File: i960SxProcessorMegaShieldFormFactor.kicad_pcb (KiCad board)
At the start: 4 copper layers, 101.6 x 53.3 mm, 42 parts, among them P1 Power, P2 Data Lines Lower, P3 Data Lines Upper, P4 Address Lines, P5 PWM, P6 Serializable Pins, P7 1284p Direct Connection, U1 74LVC16T245, U2 74AHC16373, U3 80960Sx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

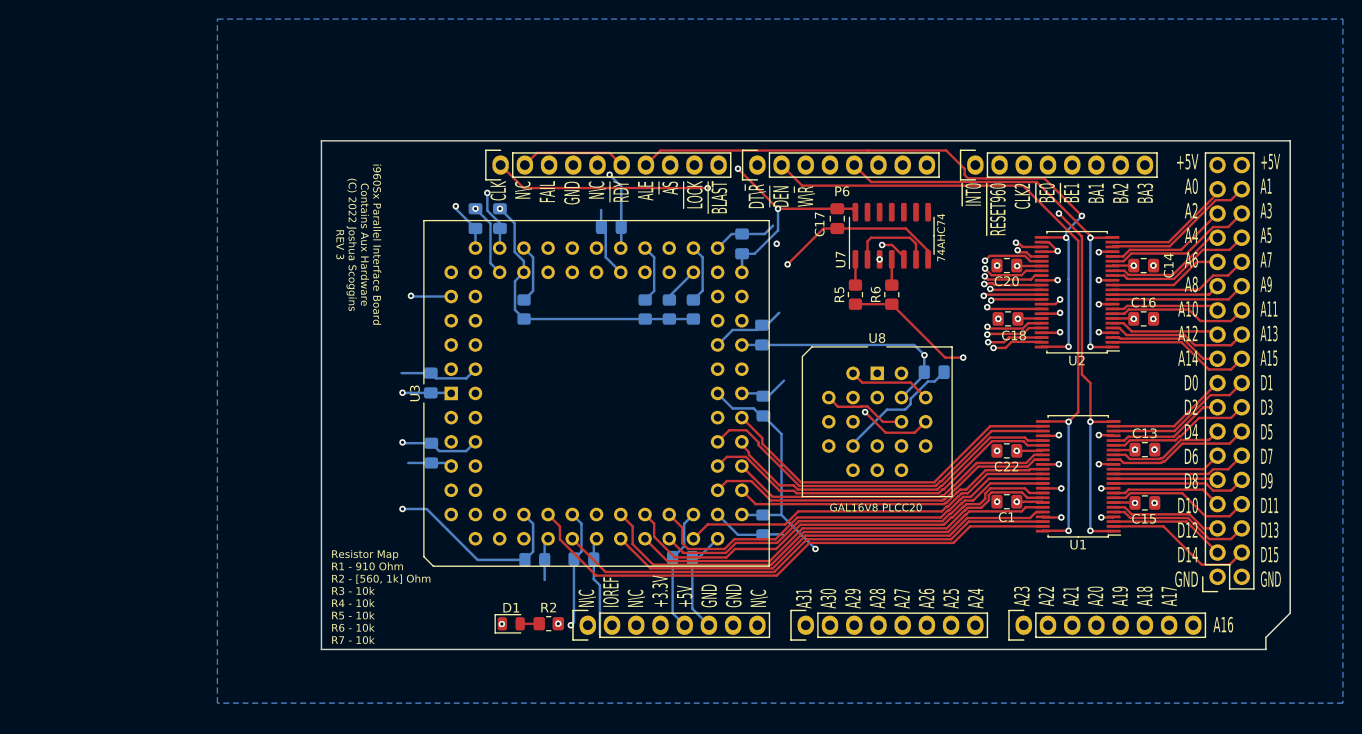
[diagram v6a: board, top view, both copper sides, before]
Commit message: Clean up all of the aux hardware and put the capacitors in the area underneath the socket
It makes it much cleaner

Also, I made sure that the ground and power planes are on all layers to
reduce complexity
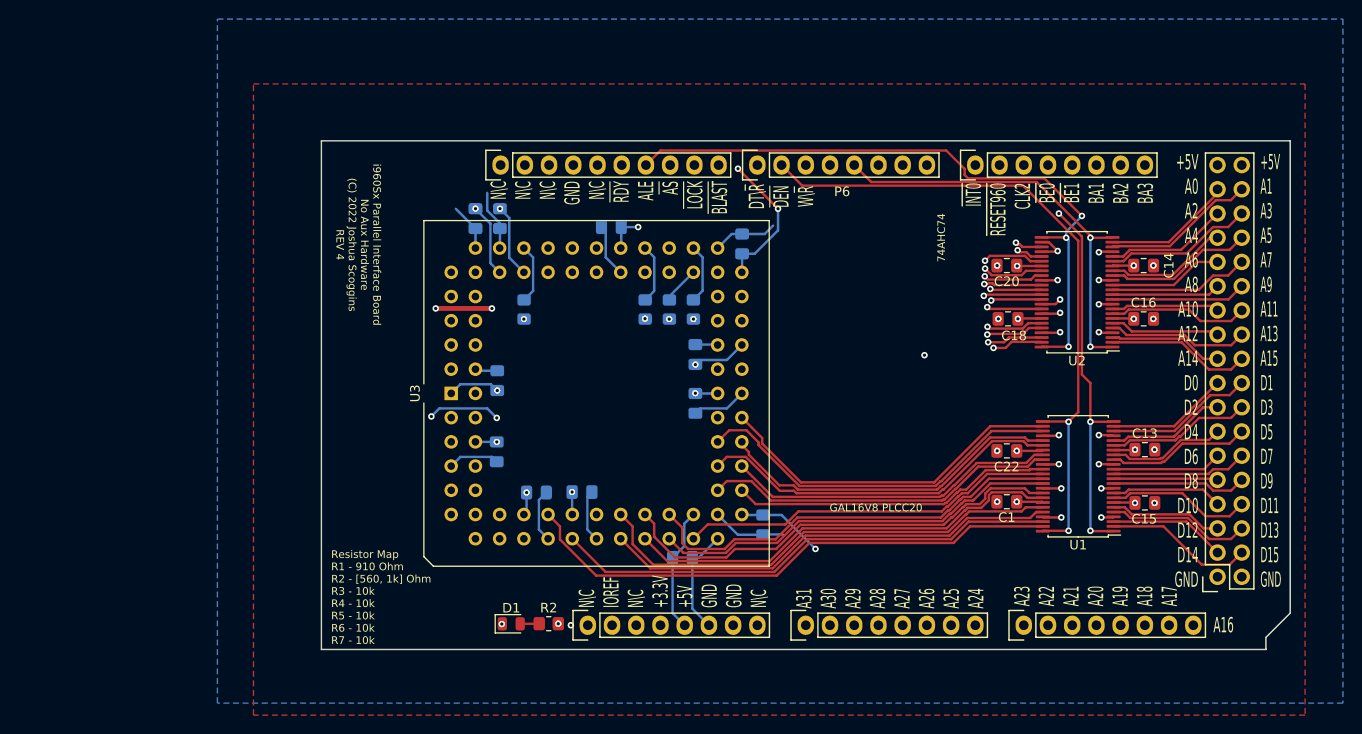
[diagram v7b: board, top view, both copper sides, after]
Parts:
- removed C17, C19: 0.1uF, Capacitor_SMD:C_0805_2012Metric_Pad1.18x1.45mm_HandSolder
- removed R5, R6: 10k, Resistor_SMD:R_0805_2012Metric_Pad1.20x1.40mm_HandSolder
- removed U7: 74AHC74, Package_SO:SOIC-14_3.9x8.7mm_P1.27mm
- removed U8: GAL16V8, Package_LCC:PLCC-20_THT-Socket
- moved C12 7.28 mm to (142.6, 90.7)
- moved C21 7.14 mm to (142.6, 95.9), turned to -90 degrees
- moved C4 7.07 mm to (125.9, 105.2)
- moved C3 7.04 mm to (130.7, 105.2)
- moved C7 6.98 mm to (121.8, 93.5)
- moved C5 6.87 mm to (121.8, 100.9)
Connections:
- P5 pad 1: /CLK_DIV2 -> unconnected-(P5-Pad1)
- P5 pad 2: /~{READY} -> unconnected-(P5-Pad2)
- P5 pad 3: /MCU_FAIL -> unconnected-(P5-Pad3)
- U3 pad 79: /~{READY960} -> /~{READY}
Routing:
- net +5V: track 200.2 -> 88.7 mm, vias 14 -> 22
- net /CLK_DIV2: track 61.3 -> 0.00 mm, vias 3 -> 0
- net /MCU_FAIL: track 60.1 -> 0.00 mm, vias 1 -> 0
- net /~{READY960}: track 58.7 -> 0.00 mm
- net GND: track 149.7 -> 105.7 mm, vias 29 -> 27
- net /~{BLAST}\~{FAIL}: track 65.3 -> 25.6 mm
- net /~{READY}: track 51.3 -> 28.4 mm
- net /~{BE0}: track 60.0 -> 40.4 mm
- net /~{BE1}: track 57.3 -> 40.4 mm
- net Net-(U7-Pad2): track 9.03 -> 0.00 mm
- net /Sheet62305775/X: track 8.70 -> 0.00 mm
- net /Sheet62305775/Z: track 8.67 -> 0.00 mm
- net /Sheet62305775/~{SR0}: track 2.70 -> 0.00 mm
- net /Sheet62305775/~{MR0}: track 2.70 -> 0.00 mm
- net /CLKO: vias 1 -> 0
- added copper zone on F.Cu, net +5V
- added copper zone on In1.Cu, net +5V
- added copper zone on In2.Cu, net GND
- removed copper zone on In2.Cu, net +5V
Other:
- board text added: "N\C N\C N\C GND N\C ~{RDY} ALE ~{AS} ~{LOCK} ~{BLAST}"
- board text added: "i960Sx Parallel Interface Board No Aux Hardware (C) 2022 Joshua Scoggins REV 4"
- board text removed: "CLK N\C FAIL GND N\C ~{RDY} ALE ~{AS} ~{LOCK} ~{BLAST}"
- board text removed: "GAL16V8 Synchronizer CLK S Z X B0 B1 BL NC NC GND NC NC NC NC NC FL X0 Z0 RDY VCC Z0.R = S X0.R = Z /RDY = X * /Z FL.R = B0 * B1 * /BL DESCRIPTION i960 Aux Hardware"
- board text removed: "i960Sx Parallel Interface Board Contains Aux Hardware (C) 2022 Joshua Scoggins REV 3"

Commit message: Finished wiring
Super easy this way :)
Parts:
- moved C10 14.5 mm to (148.3, 77.1)
- moved C11 14.5 mm to (162.0, 78.9)
- moved C12 14.5 mm to (157.1, 90.5)
- moved C2 14.5 mm to (155.7, 111.8)
- moved C21 14.5 mm to (157.1, 95.6)
- moved C4 14.5 mm to (140.4, 105.0)
- moved C6 14.5 mm to (164.2, 108.4)
- moved C7 14.5 mm to (136.3, 93.2)
- moved R3 14.5 mm to (151.8, 85.8)
- moved R4 14.5 mm to (154.4, 85.8)
- moved R7 14.5 mm to (156.9, 85.8)
- moved U3 14.5 mm to (131.5, 94.6)
- moved C5 14.5 mm to (136.2, 100.7)
- moved C8 14.5 mm to (134.0, 76.3)
- moved C9 14.5 mm to (136.6, 76.3)
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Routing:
- net VCC: track 136.8 -> 36.9 mm
- net GND: track 105.7 -> 141.8 mm, vias 27 -> 21
- net /AD11: track 111.7 -> 79.0 mm
- net /AD1: track 87.4 -> 58.0 mm
- net /AD10: track 111.4 -> 82.5 mm
- net /AD3: track 87.4 -> 58.5 mm
- net /AD2: track 81.5 -> 52.7 mm
- net /AD12: track 116.4 -> 87.7 mm
- net /AD8: track 105.5 -> 77.2 mm
- net /AD4: track 81.1 -> 53.0 mm
- net /AD9: track 101.8 -> 73.9 mm
- net /AD14: track 122.0 -> 94.2 mm
- net /AD13: track 112.1 -> 84.4 mm
- net /AD5: track 87.1 -> 59.9 mm
- net /AD15: track 131.1 -> 104.0 mm
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- added copper zone on In1.Cu, net VCC
- removed copper zone on In1.Cu, net +5V
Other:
- board text removed: "74AHC74"
- board text removed: "GAL16V8 PLCC20"
